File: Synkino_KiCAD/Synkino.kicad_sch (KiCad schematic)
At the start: 162 parts, among them J1 Pwr, J10 EYE8_OUT, J11 EYE4_OUT, J12 Eye, J13 EYE5_OUT, J2 Eye, J3 3.5mm, J4 Micro_SD_Card_Det_Hirose_DM3AT, J5 EYE1_OUT, J6 EYE6_OUT, J7 EYE2_OUT, J8 EYE7_OUT, J9 EYE3_OUT, Q1 IRF7319, Q2 BC847 o. SS8050, Q3 IRLML2244 o. AO3401A, SW1 Power, SW2 Rotary_Encoder_Switch, SW3 Reset, U1 ME6210A50PG, U10 ATMEGA328P-AU, U11 QRE1113GR, U12 QRE1113GR, U13 QRE1113GR, U14 QRE1113GR, U15 QRE1113GR, U16 QRE1113GR, U17 24LC256, U18 QRE1113GR, U2 ATMEGA328P-AU, U3 74HC4050, U4 SPIOLED128x64, U5 AP7312-1833W6-7, U6 74HC14, U7 VS1053B, U8 GS3005, U9 QRE1113GR, X1 FTDIconn, X2 ICSP, X3 FTDIconn, X4 ICSP, Y1 16Mhz, Y2 12.288MHz, Y3 16Mhz

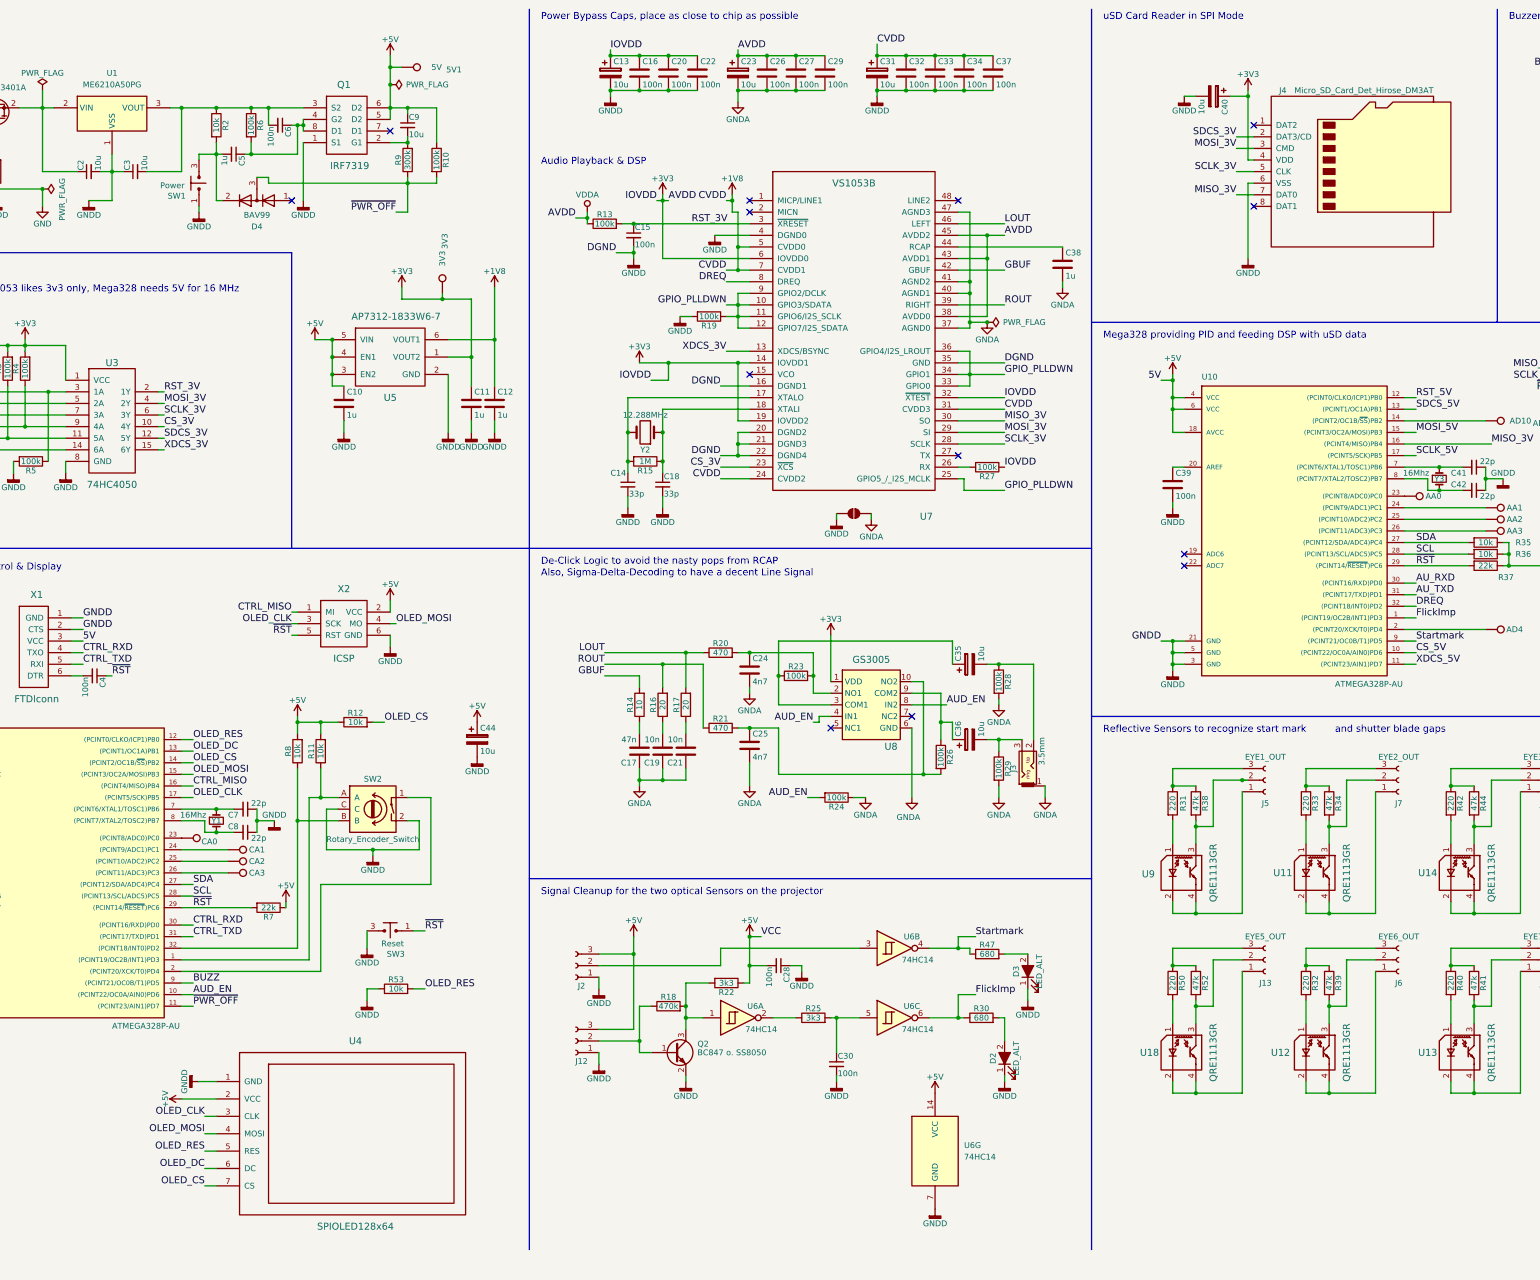
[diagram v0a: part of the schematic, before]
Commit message: all nc pins added to symbols
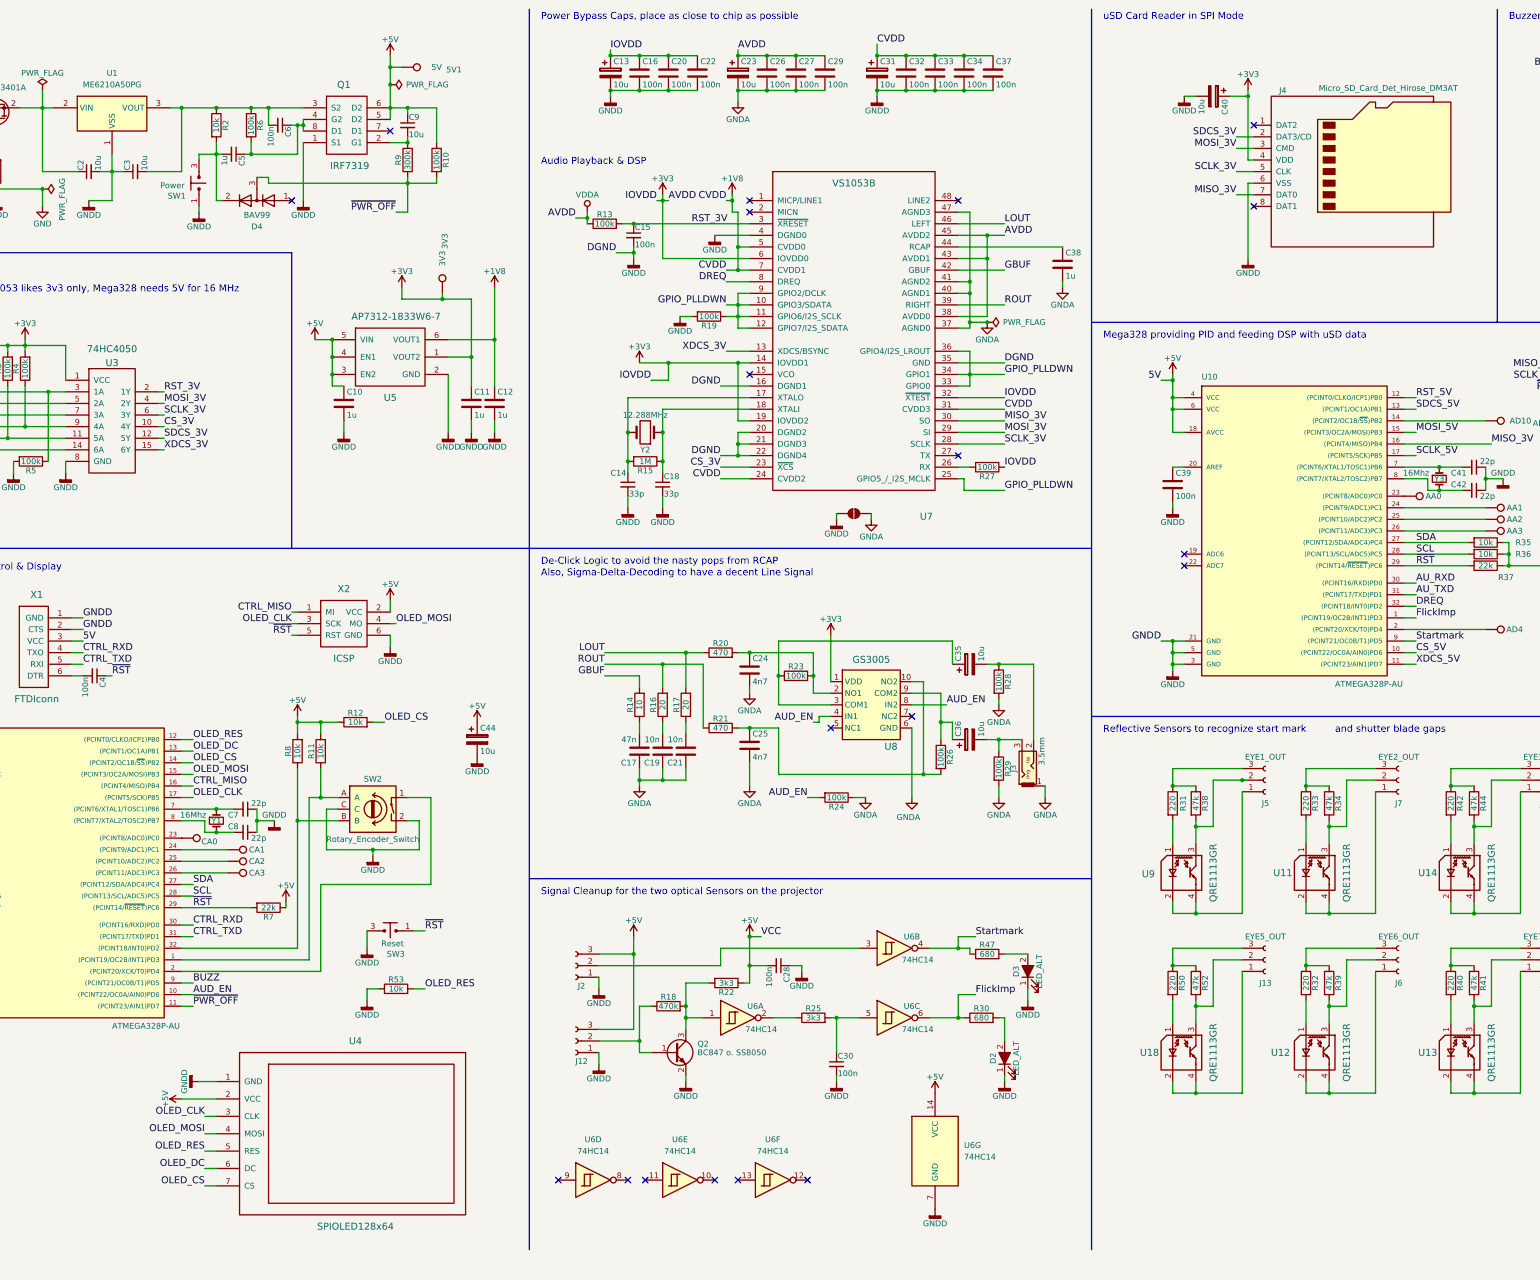
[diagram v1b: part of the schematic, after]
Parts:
- added unit 6 of U6
- added unit 4 of U6
- added unit 5 of U6
- J4: symbol Synkino:Micro_SD_Card_Det_Hirose_DM3AT -> Synkino:Micro_SD_Card_Det
- U3: symbol Synkino:74HC4050 -> 74hc4050:74HC4050
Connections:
- no-connect marks 15 -> 21

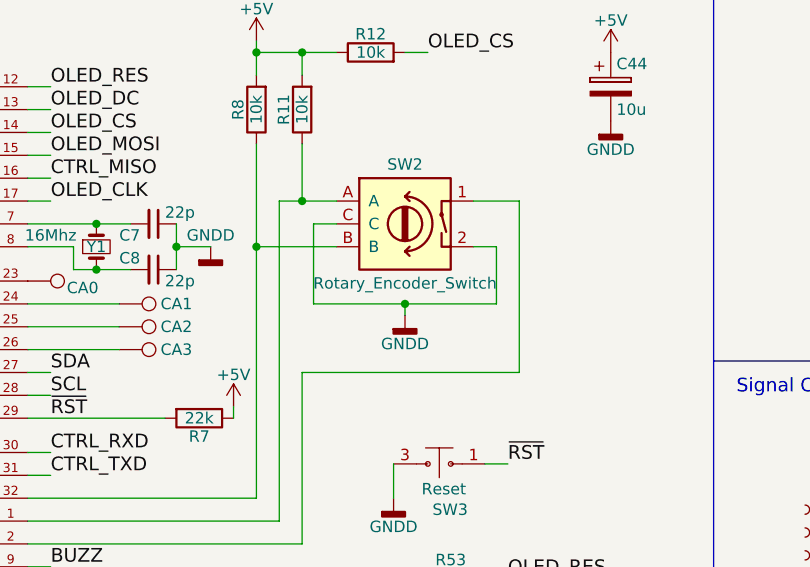
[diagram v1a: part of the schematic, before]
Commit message: 0 DRC Errors (but Warnings), ICSP fp displaced
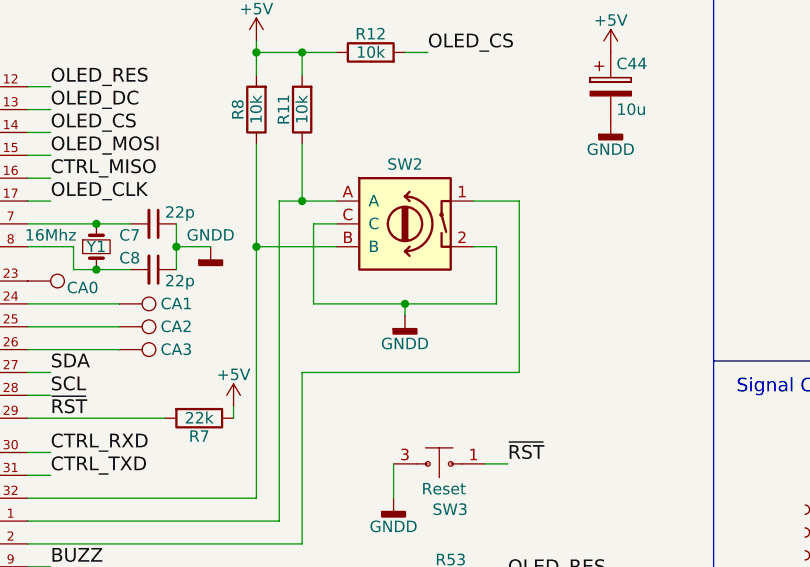
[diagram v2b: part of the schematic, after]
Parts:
- SW2: value Rotary_Encoder_Switch -> Encoder
- U11, U12, U13, U14, U15, U16, U18, U9: footprint OptoDevice:OnSemi_CASE100CY -> OptoDevice:OnSemi_CASE100CY_1-smaller
- U6: footprint (none) -> Package_SO:SOIC-14_3.9x8.7mm_P1.27mm
- X2, X4: footprint Connector_PinHeader_2.54mm:PinHeader_2x03_P2.54mm_Vertical -> Connector_PinHeader_2.54mm:PinHeader_2x03_P2.54mm_Vertical_displaced
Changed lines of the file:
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@@
 			)
 		)
-		(property "Footprint" "Connector_PinHeader_2.54mm:PinHeader_2x03_P2.54mm_Vertical"
+		(property "Footprint" "Connector_PinHeader_2.54mm:PinHeader_2x03_P2.54mm_Vertical_displaced"
 			(at 383.54 97.79 0)
 			(effects
@@
 			)
 		)
-		(property "Footprint" "Connector_PinHeader_2.54mm:PinHeader_2x03_P2.54mm_Vertical"
+		(property "Footprint" "Connector_PinHeader_2.54mm:PinHeader_2x03_P2.54mm_Vertical_displaced"
 			(at 106.68 151.13 0)
 			(effects
@@
 			)
 		)
-		(property "Value" "Rotary_Encoder_Switch"
+		(property "Value" "Encoder"
 			(at 114.3 194.564 0)
 			(effects
@@
 					(size 1.27 1.27)
 				)
+				(hide yes)
 			)
 		)
@@
 			)
 		)
-		(property "Footprint" "OptoDevice:OnSemi_CASE100CY"
+		(property "Footprint" "OptoDevice:OnSemi_CASE100CY_1-smaller"
 			(at 322.58 224.79 0)
 			(effects
@@
 			)
 		)
-		(property "Footprint" "OptoDevice:OnSemi_CASE100CY"
+		(property "Footprint" "OptoDevice:OnSemi_CASE100CY_1-smaller"
 			(at 293.37 224.79 0)
 			(effects
@@
 			)
 		)
-		(property "Footprint" "OptoDevice:OnSemi_CASE100CY"
+		(property "Footprint" "OptoDevice:OnSemi_CASE100CY_1-smaller"
 			(at 383.54 224.79 0)
 			(effects
@@
 			)
 		)
-		(property "Footprint" "OptoDevice:OnSemi_CASE100CY"
+		(property "Footprint" "OptoDevice:OnSemi_CASE100CY_1-smaller"
 			(at 354.33 224.79 0)
 			(effects
@@
 			)
 		)
-		(property "Footprint" "OptoDevice:OnSemi_CASE100CY"
+		(property "Footprint" "OptoDevice:OnSemi_CASE100CY_1-smaller"
 			(at 293.37 264.16 0)
 			(effects
@@
 			)
 		)
-		(property "Footprint" "OptoDevice:OnSemi_CASE100CY"
+		(property "Footprint" "OptoDevice:OnSemi_CASE100CY_1-smaller"
 			(at 354.33 264.16 0)
 			(effects
@@
 			)
 		)
-		(property "Footprint" "OptoDevice:OnSemi_CASE100CY"
+		(property "Footprint" "OptoDevice:OnSemi_CASE100CY_1-smaller"
 			(at 322.58 264.16 0)
 			(effects
@@
 			)
 		)
-		(property "Footprint" "OptoDevice:OnSemi_CASE100CY"
+		(property "Footprint" "OptoDevice:OnSemi_CASE100CY_1-smaller"
 			(at 383.54 264.16 0)
 			(effects
@@
 			)
 		)
-		(property "Footprint" ""
+		(property "Footprint" "Package_SO:SOIC-14_3.9x8.7mm_P1.27mm"
 			(at 201.93 269.24 0)
 			(effects
@@
 			)
 		)
-		(property "Footprint" ""
+		(property "Footprint" "Package_SO:SOIC-14_3.9x8.7mm_P1.27mm"
 			(at 162.56 269.24 0)
 			(effects
@@
 			)
 		)
-		(property "Footprint" ""
+		(property "Footprint" "Package_SO:SOIC-14_3.9x8.7mm_P1.27mm"
 			(at 181.61 269.24 0)
 			(effects

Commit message: BOM Updates, more datasheets
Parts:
- 3V3, 5V1, AA0, AA1, AA2, AA3, AD10, AD4, CA0, CA1, CA2, CA3, GND1, GND2, J3, JP1, SCL1, SDA1, SW2, U4, X1, X2, X3, X4: now left out of the parts list
- J1: LCSC (none) -> C5188442
- J10, J11, J13, J6, J7, J8, J9: Manual Assy (none) -> C5188443; now left out of the parts list
- J5: LCSC C5188443 -> (none); Manual Assy (none) -> C5188443; now left out of the parts list
- SW1: Alternative (none) -> C5377648; LCSC C5377648 -> C561258; LCSC Part C5377648 -> (none)
- SW3: Alternative (none) -> C5148353; LCSC C5148352 -> C2936025; LCSC Part C5148352 -> (none)
- U1: LCSC Part C82940 -> (none)
- U11, U12, U13, U9: Alternative (none) -> C232862; LCSC C232862 -> C81632
- U14, U15: Alternative (none) -> C232862; LCSC (none) -> C81632
- U8: LCSC Part C840037 -> (none)
